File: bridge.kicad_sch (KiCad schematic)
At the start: 1 part, among them U2 FT260Q-T

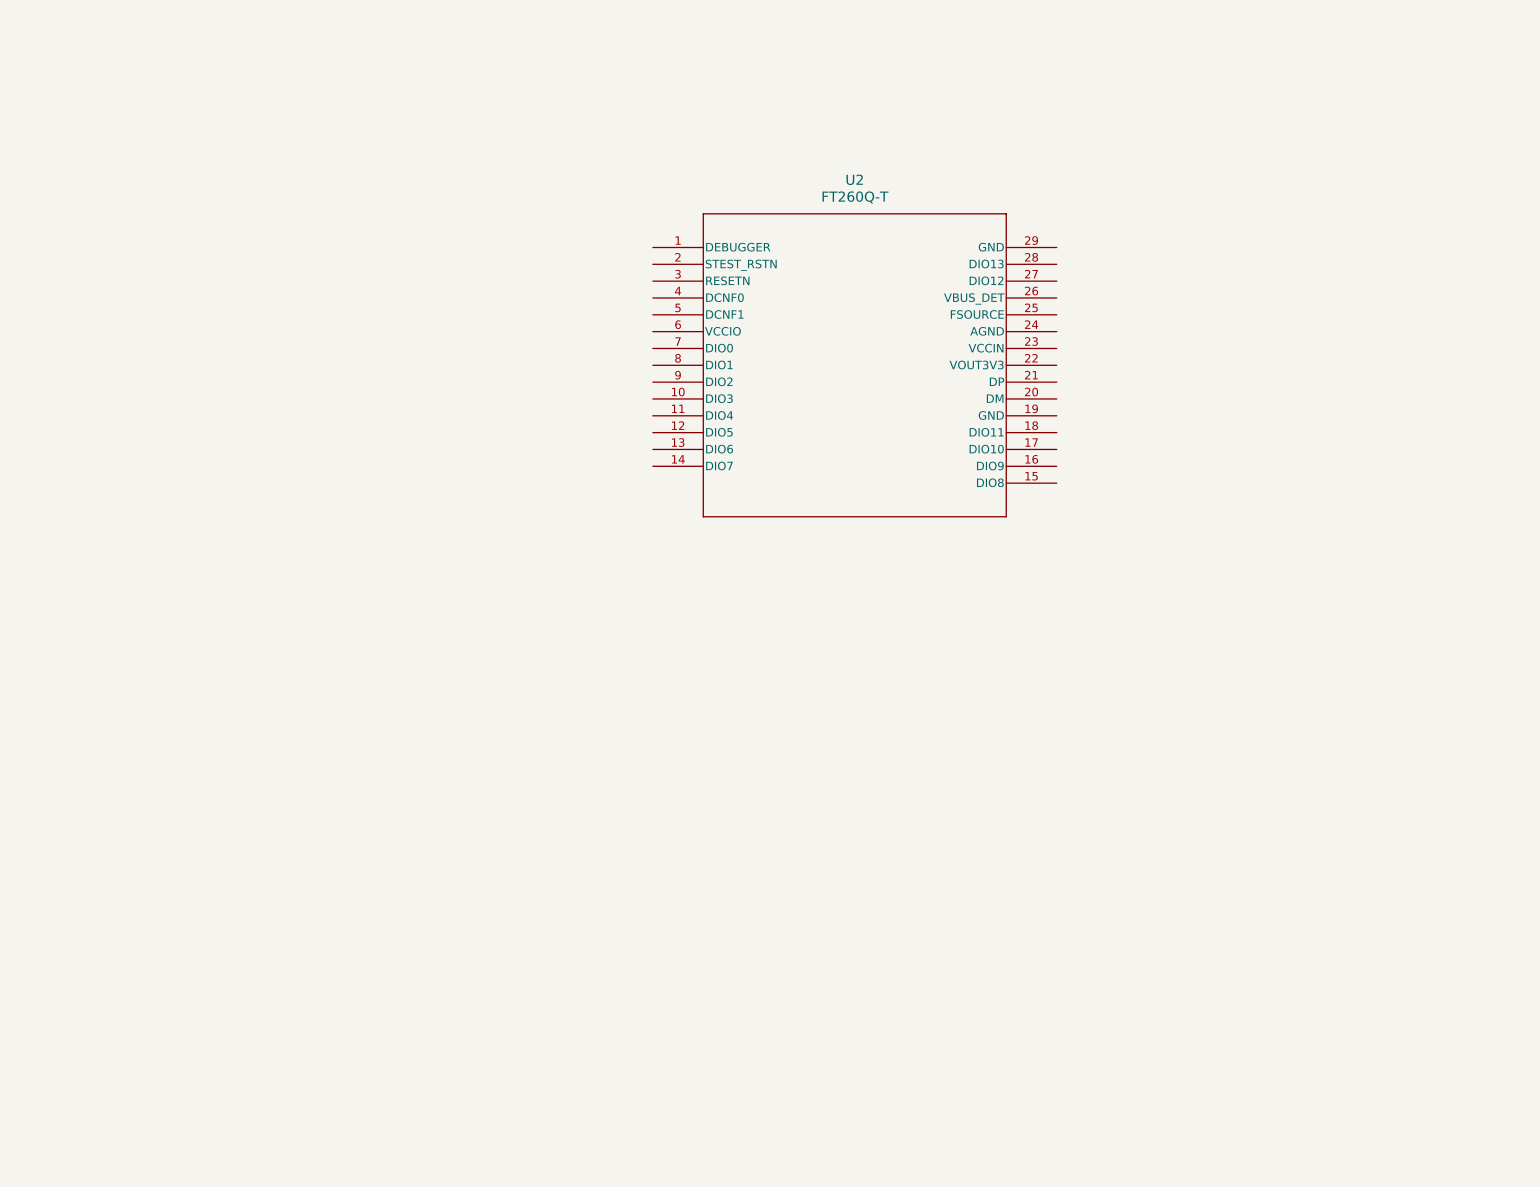
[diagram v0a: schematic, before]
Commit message: Added sensor page plus relays, and additional power
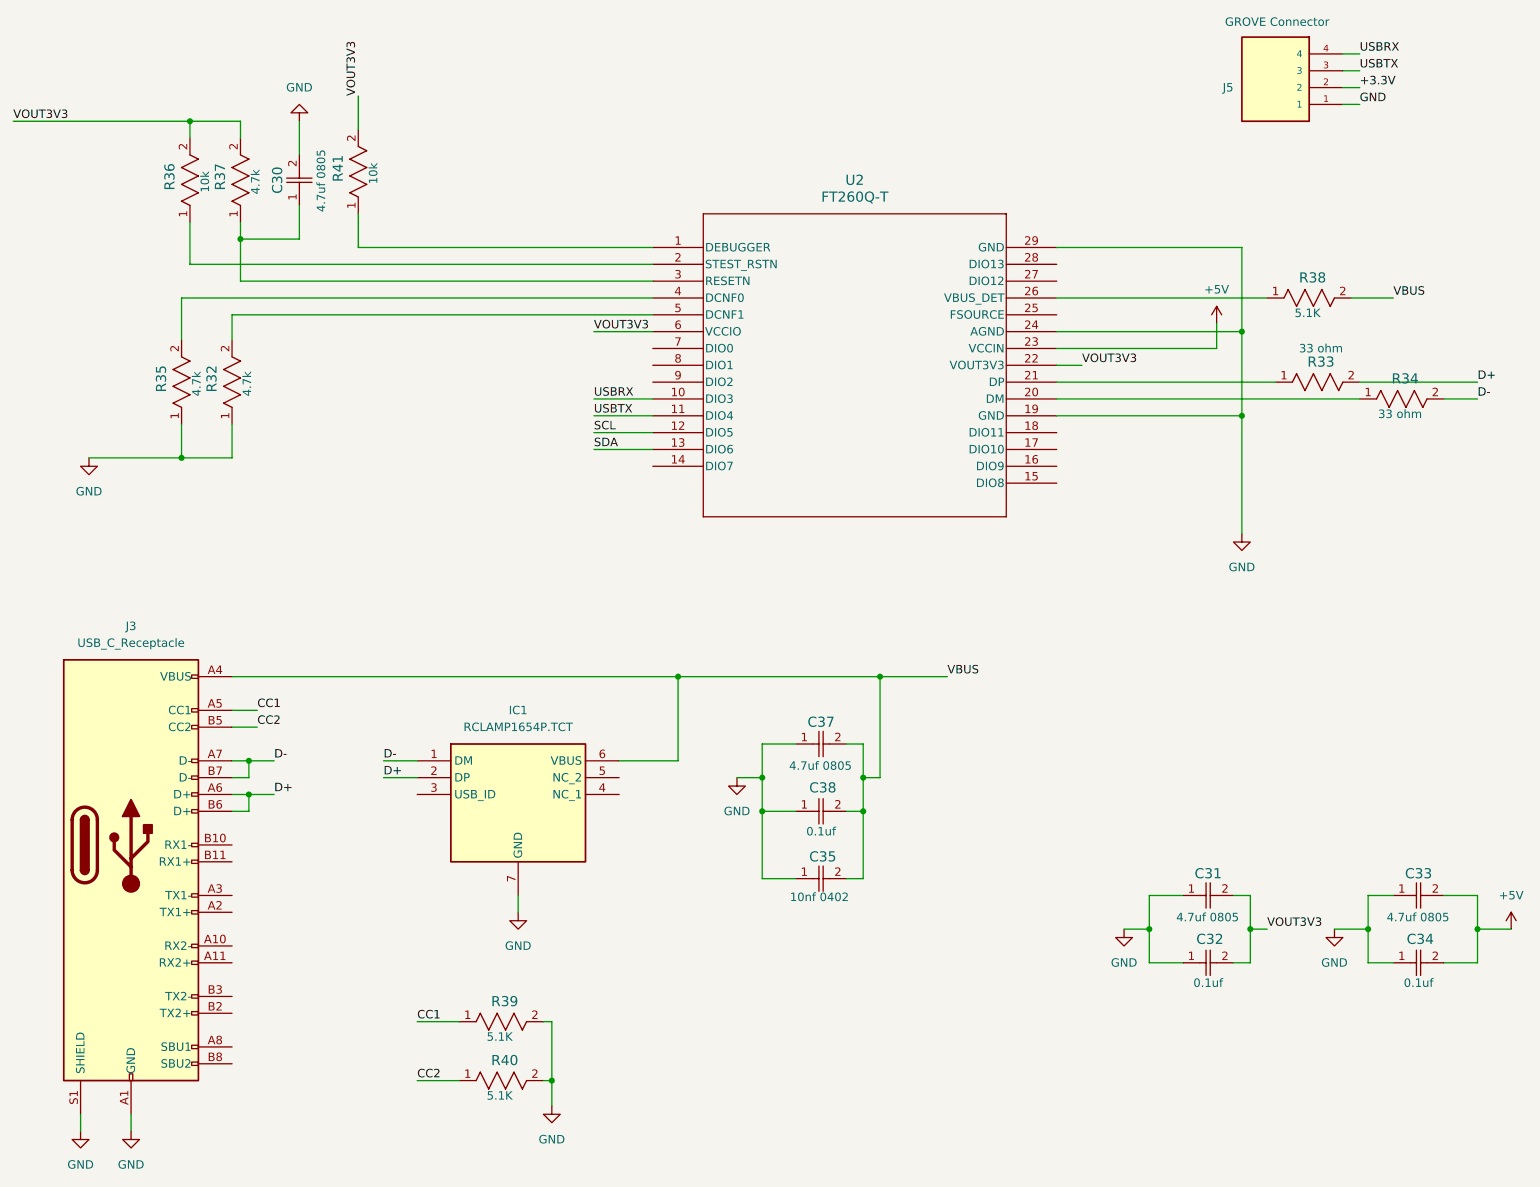
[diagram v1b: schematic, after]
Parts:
- added C30, C31, C33, C37: GRM21BR61H475KE51L, CAP_GRM21BR61H106KE43K_MUR, symbol 2025-04-06_15-56-13:GRM21BR61H106KE43K
- added C32, C34, C38: NMC0402X7R104K50TRPF, CAP_NMC0402_NIC, symbol 2025-04-20_15-51-24:NMC0402X7R104K50TRPF
- added C35: C0402C103K5REC7411, CAPC10555_55N_KEM, symbol 2025-04-13_16-32-29:C0402C105K4PAC7411
- added IC1: RCLAMP1654P.TCT, SON50P160X160X65-7N, symbol RCLAMP1654P_TCT:RCLAMP1654P.TCT
- added J3: USB_C_Receptacle, symbol Connector:USB_C_Receptacle
- added J5: GROVE Connector, 110990030:SEEED_110990030, symbol 110990030:110990030
- added R32, R35, R37: AC0402FR-134K7L, YAG_R0402_YAG, symbol 2025-04-05_21-56-13:RC0402FR-07820RL
- added R33, R34: AC0402FR-7W33RL, YAG_R0402_YAG, symbol 2025-04-05_21-56-13:RC0402FR-07820RL
- added R36, R41: AC0402FR-0710KL, YAG_R0402_YAG, symbol 2025-04-05_21-56-13:RC0402FR-07820RL
- added R38, R39, R40: AC0402FR-135K1L, YAG_R0402_YAG, symbol 2025-04-05_21-56-13:RC0402FR-07820RL
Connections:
- net at U2.1 (DEBUGGER): now also R41.1
- net USBRX: now reaches U2.10 (DIO3)
- net USBRX: now also J5.4
- net USBTX: now reaches U2.11 (DIO4)
- net USBTX: now also J5.3
- net SCL: now reaches U2.12 (DIO5)
- net SDA: now reaches U2.13 (DIO6)
- net GND: now reaches U2.19 (GND)
- net GND: now also U2.24 (AGND), U2.29 (GND), C30.2, C31.1, C32.1, C33.1, C34.1, C35.1, C37.1, C38.1, IC1.7 (GND), J3.A1 (GND), J3.A12 (GND), J3.B1 (GND), J3.B12 (GND), J3.S1 (SHIELD), J5.1, R32.1, R35.1, R39.2, R40.2
- net at U2.2 (STEST_RSTN): now also R36.1
- net at U2.20 (DM): now also R34.1
- net at U2.21 (DP): now also R33.1
- net VOUT3V3: now reaches U2.22 (VOUT3V3)
- net VOUT3V3: now also U2.6 (VCCIO), C31.2, C32.2, R36.2, R37.2, R41.2
- net +5V: now reaches U2.23 (VCCIN)
- net +5V: now also C33.2, C34.2
- net at U2.26 (VBUS_DET): now also R38.1
- net at U2.3 (RESETN): now also C30.1, R37.1
- net at U2.4 (DCNF0): now also R35.2
- net at U2.5 (DCNF1): now also R32.2
- new net +3.3V: J5.2
- new net CC1: J3.A5 (CC1), R39.1
- new net CC2: J3.B5 (CC2), R40.1
- new net D+: IC1.2 (DP), J3.A6 (D+), J3.B6 (D+), R33.2
- new net D-: IC1.1 (DM), J3.A7 (D-), J3.B7 (D-), R34.2
- new net VBUS: C35.2, C37.2, C38.2, IC1.6 (VBUS), J3.A4 (VBUS), J3.A9 (VBUS), J3.B4 (VBUS), J3.B9 (VBUS), R38.2
